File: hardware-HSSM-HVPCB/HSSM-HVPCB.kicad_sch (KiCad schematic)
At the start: 7 parts, among them J1 2086-1103, J2 2601-1110, K1 G6DN-1A-L DC12, K2 G6DN-1A-L DC12, U1 LNK3202D-TL

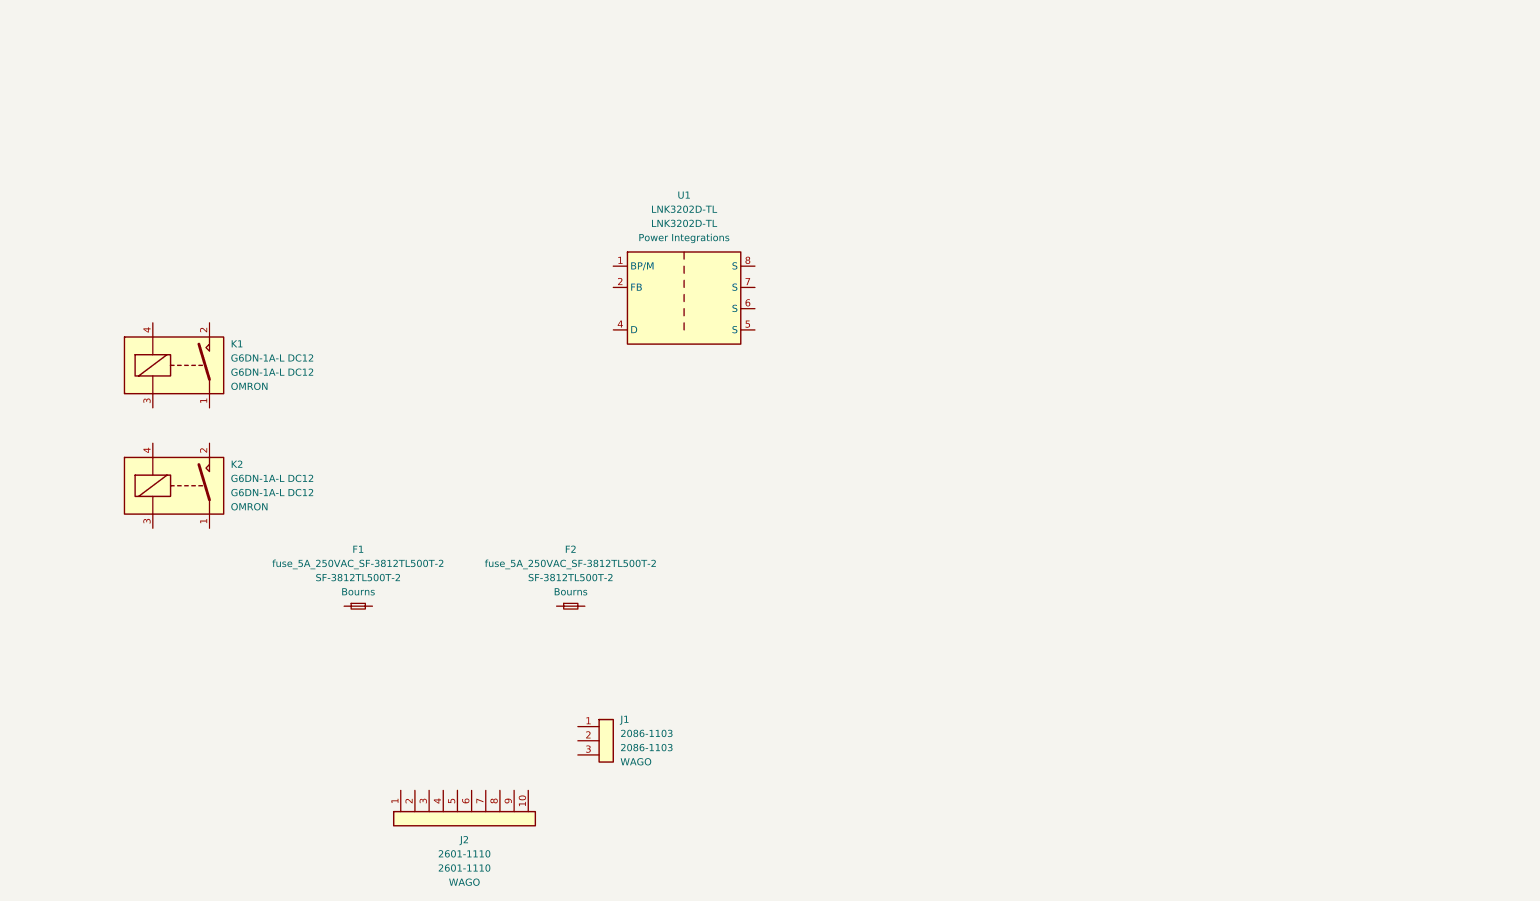
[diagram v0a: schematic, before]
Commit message: [#3] Add components to schematic
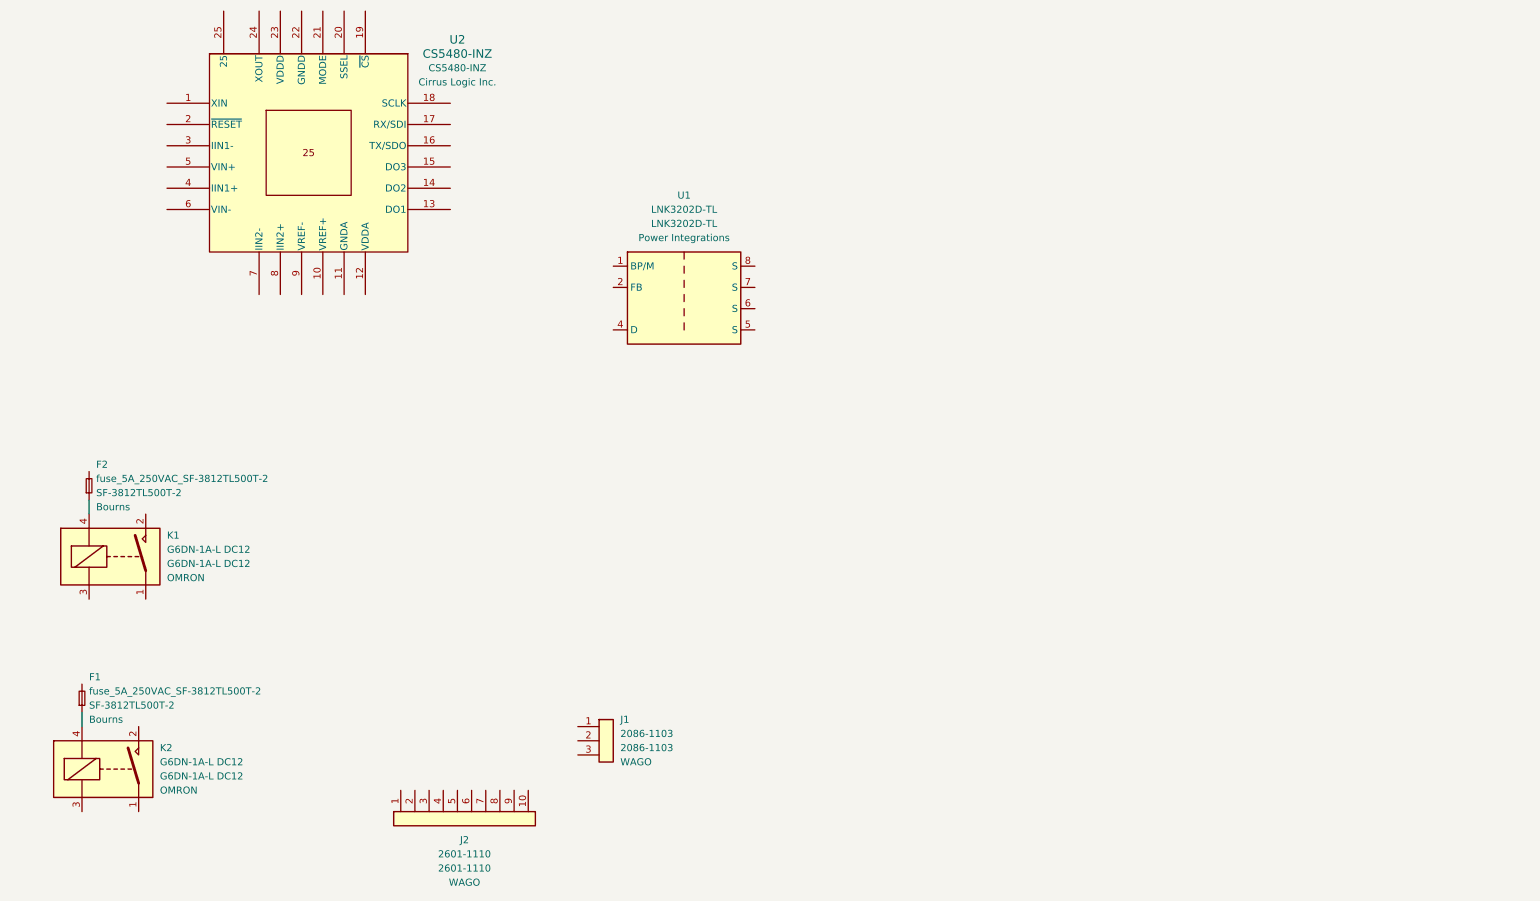
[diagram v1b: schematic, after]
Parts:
- added U2: CS5480-INZ, CIR-QFN-24, symbol HSSM-HVPCB:power_meter_CS5480-INZ
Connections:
- net at K1.4: now also F2.1
- net at K2.4: now also F1.1
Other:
- moved on the sheet: F1, F2, K1, K2
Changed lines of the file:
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@@
 	(generator_version "8.0")
 	(paper "A4")
+	(wire
+		(pts
+			(xy 35.56 156.21) (xy 35.56 158.75)
+		)
+		(stroke
+			(width 0)
+			(type default)
+		)
+	)
+	(wire
+		(pts
+			(xy 36.83 118.11) (xy 36.83 120.65)
+		)
+		(stroke
+			(width 0)
+			(type default)
+		)
+	)
+	(symbol
+		(lib_id "HSSM-HVPCB:power_meter_CS5480-INZ")
+		(at 76.2 55.88 0)
+		(unit 1)
+		(exclude_from_sim no)
+		(in_bom yes)
+		(on_board yes)
+		(dnp no)
+		(fields_autoplaced yes)
+		(property "Reference" "U2"
+			(at 102.87 35.5914 0)
+			(effects
+				(font
+					(size 1.524 1.524)
+				)
+			)
+		)
+		(property "Value" "CS5480-INZ"
+			(at 102.87 38.1314 0)
+			(effects
+				(font
+					(size 1.524 1.524)
+				)
+			)
+		)
+		(property "Footprint" "CIR-QFN-24"
+			(at 73.406 55.372 0)
+			(effects
+				(font
+					(size 1.27 1.27)
+					(italic yes)
+				)
+				(hide yes)
+			)
+		)
+		(property "Datasheet" "https://d3uzseaevmutz1.cloudfront.net/pubs/proDatasheet/CS5480_F3.pdf"
+			(at 73.406 55.372 0)
+			(effects
+				(font
+					(size 1.27 1.27)
+					(italic yes)
+				)
+				(hide yes)
+			)
+		)
+		(property "Description" "IC ENERGY METER 3-CH 24QFN"
+			(at 73.406 55.372 0)
+			(effects
+				(font
+					(size 1.27 1.27)
+				)
+				(hide yes)
+			)
+		)
+		(property "MPN" "CS5480-INZ"
+			(at 102.87 40.6714 0)
+			(effects
+				(font
+					(size 1.27 1.27)
+				)
+			)
+		)
+		(property "Manufacturer" "Cirrus Logic Inc."
+			(at 102.87 43.2114 0)
+			(effects
+				(font
+					(size 1.27 1.27)
+				)
+			)
+		)
+		(pin "10"
+		)
+		(pin "1"
+		)
+		(pin "12"
+		)
+		(pin "13"
+		)
+		(pin "14"
+		)
+		(pin "15"
+		)
+		(pin "16"
+		)
+		(pin "17"
+		)
+		(pin "18"
+		)
+		(pin "20"
+		)
+		(pin "21"
+		)
+		(pin "22"
+		)
+		(pin "23"
+		)
+		(pin "25"
+		)
+		(pin "3"
+		)
+		(pin "4"
+		)
+		(pin "5"
+		)
+		(pin "6"
+		)
+		(pin "7"
+		)
+		(pin "8"
+		)
+		(pin "9"
+		)
+		(pin "19"
+		)
+		(pin "2"
+		)
+		(pin "24"
+		)
+		(pin "11"
+		)
+		(instances
+			(project ""
+				(path "/e1056638-7c6b-48e4-9e2e-c0f7b783eee5"
+					(reference "U2")
+					(unit 1)
+				)
+			)
+		)
+	)
 	(symbol
 		(lib_id "HSSM-HVPCB:G6DN-1A-L DC12")
-		(at 53.34 93.98 0)
+		(at 41.91 128.27 0)
 		(unit 1)
 		(exclude_from_sim no)
@@
 		(fields_autoplaced yes)
 		(property "Reference" "K1"
-			(at 62.23 90.1699 0)
+			(at 50.8 124.4599 0)
 			(effects
 				(font
@@
 		)
 		(property "Value" "G6DN-1A-L DC12"
-			(at 62.23 92.7099 0)
+			(at 50.8 126.9999 0)
 			(effects
 				(font
@@
 		)
 		(property "Footprint" ""
-			(at 62.23 95.25 0)
+			(at 50.8 129.54 0)
 			(effects
 				(font
@@
 		)
 		(property "Datasheet" "https://www.mouser.pl/datasheet/2/307/en-g6dn-838135.pdf"
-			(at 53.34 93.98 0)
+			(at 41.91 128.27 0)
 			(effects
 				(font
@@
 		)
 		(property "Description" "Standex Meder DIP reed relay, SPST, Closing Contact"
-			(at 53.34 93.98 0)
+			(at 41.91 128.27 0)
 			(effects
 				(font
@@
 		)
 		(property "MPN" "G6DN-1A-L DC12"
-			(at 62.23 95.2499 0)
+			(at 50.8 129.5399 0)
 			(effects
 				(font
@@
 		)
 		(property "Manufacturer" "OMRON"
-			(at 62.23 97.7899 0)
+			(at 50.8 132.0799 0)
 			(effects
 				(font
@@
 	(symbol
 		(lib_id "HSSM-HVPCB:G6DN-1A-L DC12")
-		(at 53.34 115.57 0)
+		(at 40.64 166.37 0)
 		(unit 1)
 		(exclude_from_sim no)
@@
 		(fields_autoplaced yes)
 		(property "Reference" "K2"
-			(at 62.23 111.7599 0)
+			(at 49.53 162.5599 0)
 			(effects
 				(font
@@
 		)
 		(property "Value" "G6DN-1A-L DC12"
-			(at 62.23 114.2999 0)
+			(at 49.53 165.0999 0)
 			(effects
 				(font
@@
 		)
 		(property "Footprint" ""
-			(at 62.23 116.84 0)
+			(at 49.53 167.64 0)
 			(effects
 				(font
@@
 		)
 		(property "Datasheet" "https://www.mouser.pl/datasheet/2/307/en-g6dn-838135.pdf"
-			(at 53.34 115.57 0)
+			(at 40.64 166.37 0)
 			(effects
 				(font
@@
 		)
 		(property "Description" "Standex Meder DIP reed relay, SPST, Closing Contact"
-			(at 53.34 115.57 0)
+			(at 40.64 166.37 0)
 			(effects
 				(font
@@
 		)
 		(property "MPN" "G6DN-1A-L DC12"
-			(at 62.23 116.8399 0)
+			(at 49.53 167.6399 0)
 			(effects
 				(font
@@
 		)
 		(property "Manufacturer" "OMRON"
-			(at 62.23 119.3799 0)
+			(at 49.53 170.1799 0)
 			(effects
 				(font
@@
 	(symbol
 		(lib_id "HSSM-HVPCB:fuse_5A_250VAC_SF-3812TL500T-2")
-		(at 85.09 137.16 0)
+		(at 35.56 153.67 90)
 		(unit 1)
 		(exclude_from_sim no)
@@
 		(fields_autoplaced yes)
 		(property "Reference" "F1"
-			(at 85.09 127 0)
-			(effects
-				(font
-					(size 1.27 1.27)
-				)
+			(at 36.83 149.8599 90)
+			(effects
+				(font
+					(size 1.27 1.27)
+				)
+				(justify right)
 			)
 		)
 		(property "Value" "fuse_5A_250VAC_SF-3812TL500T-2"
-			(at 85.09 129.54 0)
-			(effects
-				(font
-					(size 1.27 1.27)
-				)
+			(at 36.83 152.3999 90)
+			(effects
+				(font
+					(size 1.27 1.27)
+				)
+				(justify right)
 			)
 		)
 		(property "Footprint" ""
-			(at 85.09 137.16 0)
+			(at 35.56 153.67 0)
 			(effects
 				(font
@@
 		)
 		(property "Datasheet" "https://www.bourns.com/docs/product-datasheets/sf-3812tl-t.pdf"
-			(at 85.09 137.16 0)
+			(at 35.56 153.67 0)
 			(effects
 				(font
@@
 		)
 		(property "Description" "fuse_5A_250VAC_SF-3812TL500T-2"
-			(at 85.09 137.16 0)
+			(at 35.56 153.67 0)
 			(effects
 				(font
@@
 		)
 		(property "MPN" "SF-3812TL500T-2"
-			(at 85.09 132.08 0)
-			(effects
-				(font
-					(size 1.27 1.27)
-				)
+			(at 36.83 154.9399 90)
+			(effects
+				(font
+					(size 1.27 1.27)
+				)
+				(justify right)
 			)
 		)
 		(property "Manufacturer" "Bourns"
-			(at 85.09 134.62 0)
-			(effects
-				(font
-					(size 1.27 1.27)
-				)
+			(at 36.83 157.4799 90)
+			(effects
+				(font
+					(size 1.27 1.27)
+				)
+				(justify right)
 			)
 		)
@@
 	(symbol
 		(lib_id "HSSM-HVPCB:fuse_5A_250VAC_SF-3812TL500T-2")
-		(at 123.19 137.16 0)
+		(at 36.83 115.57 90)
 		(unit 1)
 		(exclude_from_sim no)
@@
 		(fields_autoplaced yes)
 		(property "Reference" "F2"
-			(at 123.19 127 0)
-			(effects
-				(font
-					(size 1.27 1.27)
-				)
+			(at 38.1 111.7599 90)
+			(effects
+				(font
+					(size 1.27 1.27)
+				)
+				(justify right)
 			)
 		)
 		(property "Value" "fuse_5A_250VAC_SF-3812TL500T-2"
-			(at 123.19 129.54 0)
-			(effects
-				(font
-					(size 1.27 1.27)
-				)
+			(at 38.1 114.2999 90)
+			(effects
+				(font
+					(size 1.27 1.27)
+				)
+				(justify right)
 			)
 		)
 		(property "Footprint" ""
-			(at 123.19 137.16 0)
+			(at 36.83 115.57 0)
 			(effects
 				(font
@@
 		)
 		(property "Datasheet" "https://www.bourns.com/docs/product-datasheets/sf-3812tl-t.pdf"
-			(at 123.19 137.16 0)
+			(at 36.83 115.57 0)
 			(effects
 				(font
@@
 		)
 		(property "Description" "fuse_5A_250VAC_SF-3812TL500T-2"
-			(at 123.19 137.16 0)
+			(at 36.83 115.57 0)
 			(effects
 				(font
@@
 		)
 		(property "MPN" "SF-3812TL500T-2"
-			(at 123.19 132.08 0)
-			(effects
-				(font
-					(size 1.27 1.27)
-				)
+			(at 38.1 116.8399 90)
+			(effects
+				(font
+					(size 1.27 1.27)
+				)
+				(justify right)
 			)
 		)
 		(property "Manufacturer" "Bourns"
-			(at 123.19 134.62 0)
-			(effects
-				(font
-					(size 1.27 1.27)
-				)
-			)
-		)
+			(at 38.1 119.3799 90)
+			(effects
+				(font
+					(size 1.27 1.27)
+				)
+				(justify right)
+			)
+		)

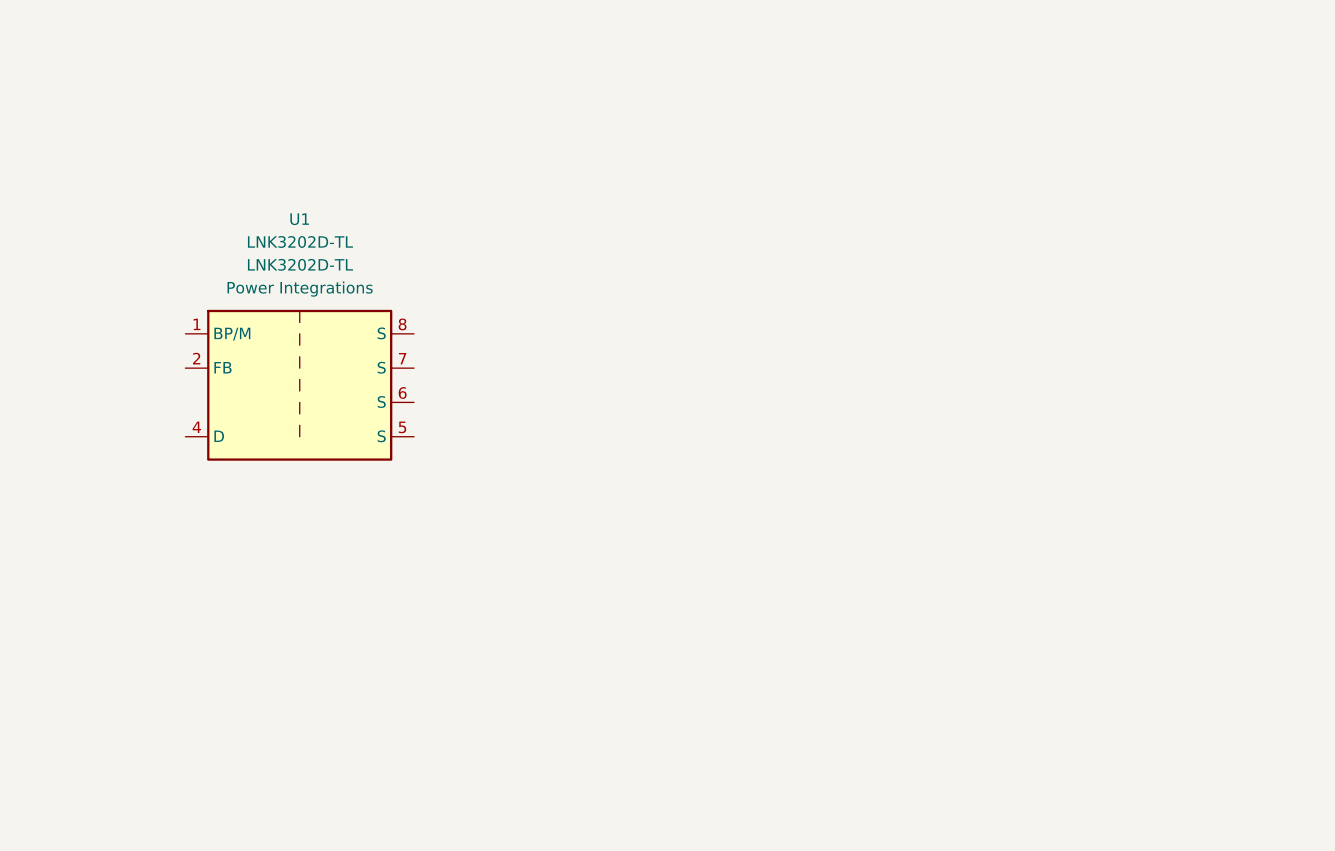
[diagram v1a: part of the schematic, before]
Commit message: [#3] SCH LNK3204 connections WIP
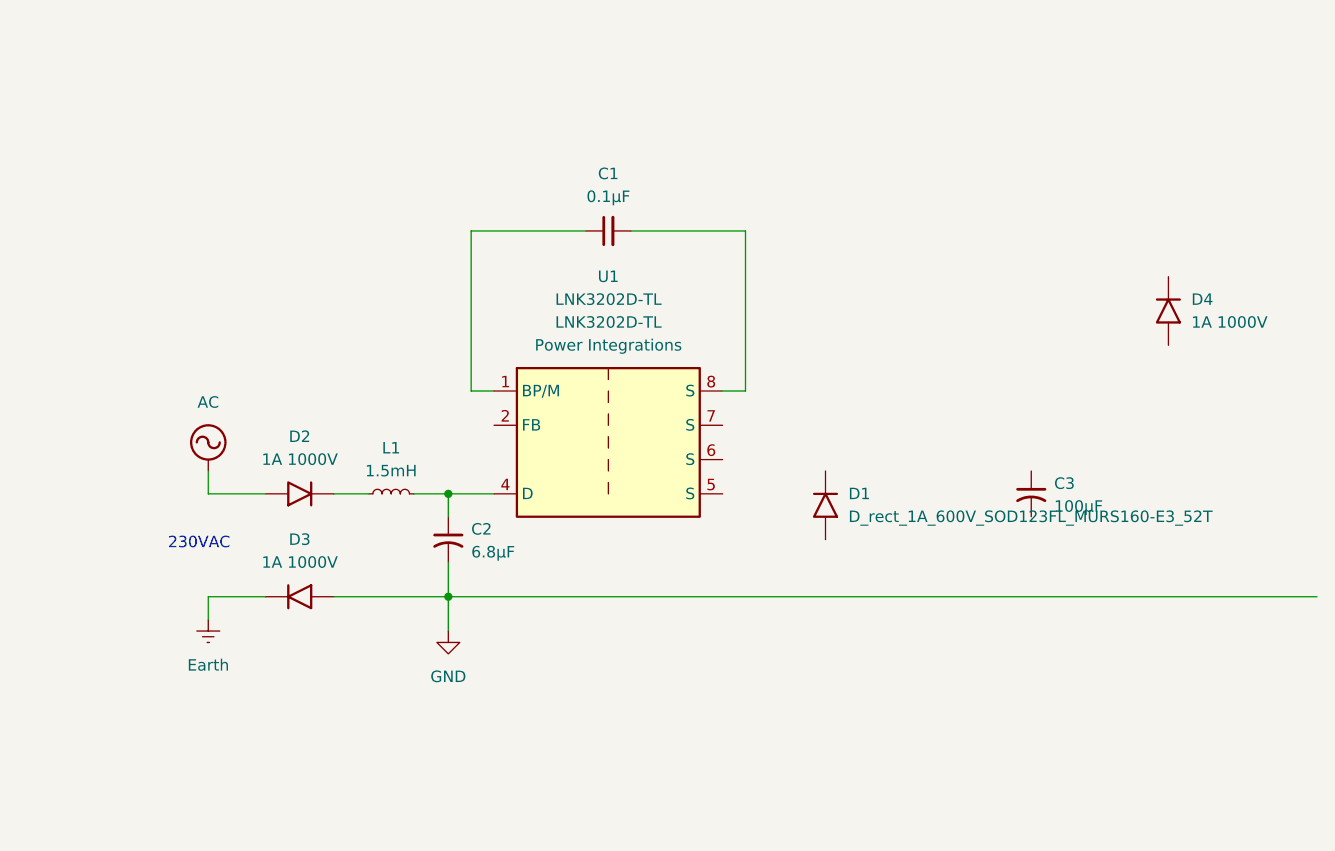
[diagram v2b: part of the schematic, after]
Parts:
- added C1: C_0u1_10pct_16V_0402_GRM155R71C104KA88J, HSSM-HVPCB:C_0402, symbol HSSM-HVPCB:C_0u1_10pct_16V_0402_GRM155R71C104KA88J
- added C2: C_6u8_20pct_400V_8mm_WCAP-ATG5_860021374009, HSSM-HVPCB:C_Radial_D8_L14_P3.5, symbol HSSM-HVPCB:C_6u8_20pct_400V_8mm_WCAP-ATG5_860021374009
- added C3: C_100uF_20pct_16V_5mm_WCAP-ATG5_860020372006, HSSM-HVPCB:C_Radial_D5_L11_P2, symbol HSSM-HVPCB:C_100uF_20pct_16V_5mm_WCAP-ATG5_860020372006
- added D1: D_rect_1A_600V_SOD123FL_MURS160-E3_52T, HSSM-HVPCB:D_SOD123FL, symbol HSSM-HVPCB:D_rect_1A_600V_SOD123FL_MURS160-E3_52T
- added D2, D3, D4: D_rect_1A_1000V_SOD123_1N4007W, HSSM-HVPCB:D_SOD123, symbol HSSM-HVPCB:D_rect_1A_1000V_SOD123_1N4007W
- added L1: L_1.5mH_20pct_1500uH_LPS4012-155MRC, HSSM-HVPCB:L_4.0x4.0mm, symbol HSSM-HVPCB:L_1.5mH_20pct_1500uH_LPS4012-155MRC
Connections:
- net at U1.1 (BP/M): now also C1.1
- net at U1.4 (D): now also C2.1, L1.2
- net at U1.8 (S): now also C1.2
- new net: D2.1 (K), L1.1
- new net AC: D2.2 (A)
- new net Earth: D3.1 (K)
- new net GND: C2.2, D3.2 (A)
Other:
- note added: "230VAC"
- moved on the sheet: U1
